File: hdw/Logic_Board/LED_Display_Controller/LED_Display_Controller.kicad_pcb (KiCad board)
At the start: 4 copper layers, 743 parts, among them J1101 USB_B_Mini, J1401 Encoder Ext, J1601 POS5P EXT, J1602 POS5P PGOOD, J1603 POS5P_THWN, J1604 POS5P_RUN, J201 +12V IN, J202 GND IN, J203 +12V IN AUX, J204 Master Power SW, J2901 STRING 1, J2902 STRING 2, J2903 STRING 3, J2904 STRING 4, J3001 USB UART, J3002 WIFI UART, J3003 FLASH SPI, J3004 Panel TP, J501 PICKIT3, J901 ESP8266 Socket, Q201 IPC100N04S51R7ATMA1, Q202 IPC100N04S51R7ATMA1, Q501 BSS214NW, Q901 BSS214NW, SW1401 Display Enable, SW1402 Brightness/Enable, SW501 MRST, U1001 ISO7321C, U1101 LT6700-1-S6, U1102 FT234XD, U1103 74LVC1G06, U1104 TPD3S014DBVR, U1201 74LVC1G06, U1202 74LVC1G06, U1203 74LVC1G06, U1204 74LVC1G06, U1205 74LVC1G06, U1206 74LVC1G06, U1207 74LVC1G06, U1301 74LVC1G06, U1302 74LVC1G06, U1303 74LVC1G06, U1304 74LVC1G06, U1401 MAX6816, U1402 74LVC2G14, U1403 74LVC1G79, U1601 LM1117-ADJ, U1602 NUP2202, U1603 74LVC1G17, U1604 74LVC1G17, U1605 74LVC1G17, U1606 NUP2202, U1701 CY7C1010DV33, U1801 SST25PF020B, U1901 SST25PF020B, U2001 SST25PF020B, U201 LTC4365DDB, U2101 SST25PF020B, U2201 SST25PF020B, U2301 SST25PF020B, U2401 SST25PF020B, U2501 SST25PF020B, U2601 74HCT541, U2602 74HCT541, U2701 74HCT541, U2702 74HCT541, U2801 74LVC1G32, U2802 74HCT541, U301 LTC3605A_UF, U401 LTC3624DD, U601 PIC32MZ2048EFH144_IPL

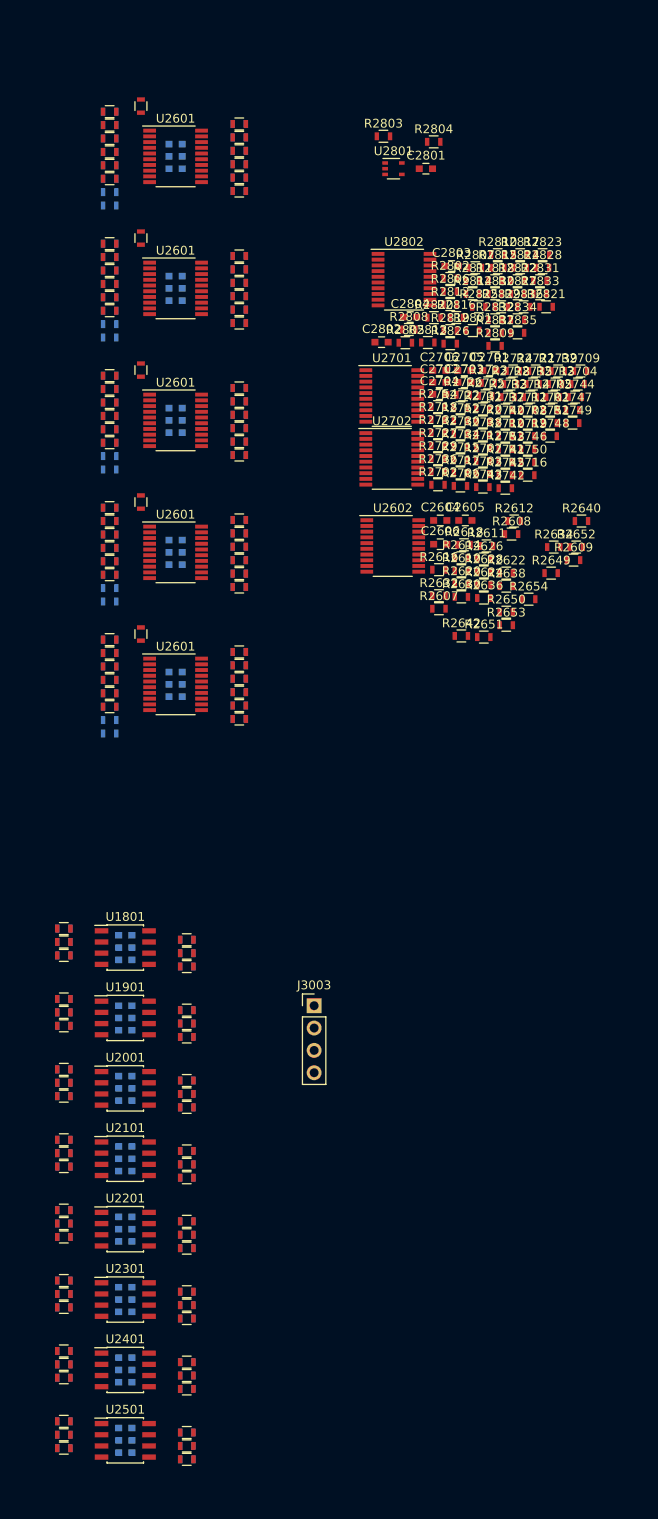
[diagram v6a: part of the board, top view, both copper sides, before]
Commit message: Fixed reference designators for level shifting/flash copies
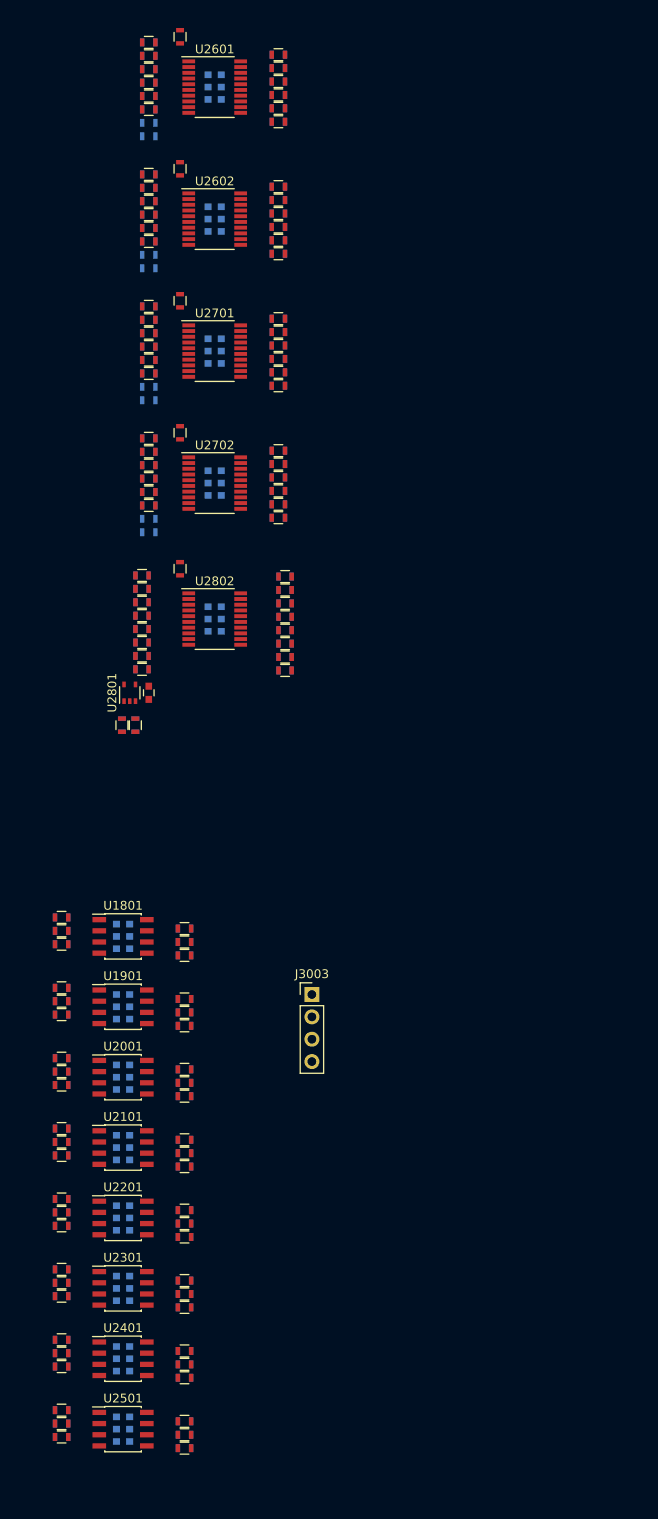
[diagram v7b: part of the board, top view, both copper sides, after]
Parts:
- removed the C2601 at (129.0, 96.7)
- removed the C2601 at (129.0, 81.7)
- removed the C2601 at (129.0, 66.7)
- removed the C2601 at (129.0, 51.7)
- removed the C2602 at (129.0, 98.1)
- removed the C2602 at (129.0, 83.1)
- removed the C2602 at (129.0, 68.1)
- removed the C2602 at (129.0, 53.1)
- removed the C2603 at (129.0, 99.5)
- removed the C2603 at (129.0, 84.5)
- removed the C2603 at (129.0, 69.5)
- removed the C2603 at (129.0, 54.5)
- removed the R2601 at (121.5, 93.0)
- removed the R2601 at (121.5, 78.0)
- removed the R2601 at (121.5, 63.0)
- removed the R2601 at (121.5, 48.0)
- removed the R2602 at (121.5, 94.5)
- removed the R2602 at (121.5, 79.5)
- removed the R2602 at (121.5, 64.5)
- removed the R2602 at (121.5, 49.5)
- removed the R2603 at (121.5, 96.1)
- removed the R2603 at (121.5, 81.1)
- removed the R2603 at (121.5, 66.1)
- removed the R2603 at (121.5, 51.1)
- removed the R2604 at (121.5, 97.6)
- removed the R2604 at (121.5, 82.6)
- removed the R2604 at (121.5, 67.6)
- removed the R2604 at (121.5, 52.6)
- removed the R2605 at (121.5, 99.1)
- removed the R2605 at (121.5, 84.1)
- removed the R2605 at (121.5, 69.1)
- removed the R2605 at (121.5, 54.1)
- removed the R2606 at (121.5, 100.6)
- removed the R2606 at (121.5, 85.6)
- removed the R2606 at (121.5, 70.6)
- removed the R2606 at (121.5, 55.6)
- removed the R2613 at (125.1, 92.4)
- removed the R2613 at (125.1, 77.4)
- removed the R2613 at (125.1, 62.4)
- removed the R2613 at (125.1, 47.4)
- removed the R2615 at (121.5, 93.0)
- removed the R2615 at (121.5, 78.0)
- removed the R2615 at (121.5, 63.0)
- removed the R2615 at (121.5, 48.0)
- removed the R2617 at (121.5, 94.5)
- removed the R2617 at (121.5, 79.5)
- removed the R2617 at (121.5, 64.5)
- removed the R2617 at (121.5, 49.5)
- removed the R2619 at (121.5, 96.1)
- removed the R2619 at (121.5, 81.1)
- removed the R2619 at (121.5, 66.1)
- removed the R2619 at (121.5, 51.1)
- removed the R2621 at (121.5, 97.6)
- removed the R2621 at (121.5, 82.6)
- removed the R2621 at (121.5, 67.6)
- removed the R2621 at (121.5, 52.6)
- removed the R2623 at (121.5, 99.1)
- removed the R2623 at (121.5, 84.1)
- removed the R2623 at (121.5, 69.1)
- removed the R2623 at (121.5, 54.1)
- removed the R2625 at (121.5, 100.6)
- removed the R2625 at (121.5, 85.6)
- removed the R2625 at (121.5, 70.6)
- removed the R2625 at (121.5, 55.6)
- removed the R2627 at (121.5, 102.2)
- removed the R2627 at (121.5, 87.2)
- removed the R2627 at (121.5, 72.2)
- removed the R2627 at (121.5, 57.2)
- removed the R2629 at (121.5, 103.7)
- removed the R2629 at (121.5, 88.7)
- removed the R2629 at (121.5, 73.7)
- removed the R2629 at (121.5, 58.7)
- removed the R2631 at (136.3, 102.0)
- removed the R2631 at (136.3, 87.0)
- removed the R2631 at (136.3, 72.0)
- removed the R2631 at (136.3, 57.0)
- removed the R2633 at (136.3, 100.5)
- removed the R2633 at (136.3, 85.5)
- removed the R2633 at (136.3, 70.5)
- removed the R2633 at (136.3, 55.5)
- removed the R2635 at (136.3, 99.0)
- removed the R2635 at (136.3, 84.0)
- removed the R2635 at (136.3, 69.0)
- removed the R2635 at (136.3, 54.0)
- removed the R2637 at (136.3, 97.5)
- removed the R2637 at (136.3, 82.5)
- removed the R2637 at (136.3, 67.5)
- removed the R2637 at (136.3, 52.5)
- removed the R2639 at (136.3, 95.9)
- removed the R2639 at (136.3, 80.9)
- removed the R2639 at (136.3, 65.9)
- removed the R2639 at (136.3, 50.9)
- removed the R2641 at (136.3, 94.4)
- removed the R2641 at (136.3, 79.4)
- removed the R2641 at (136.3, 64.4)
- removed the R2641 at (136.3, 49.4)
- removed the R2643 at (136.3, 94.4)
- removed the R2643 at (136.3, 79.4)
- removed the R2643 at (136.3, 64.4)
- removed the R2643 at (136.3, 49.4)
- removed the R2644 at (136.3, 95.9)
- removed the R2644 at (136.3, 80.9)
- removed the R2644 at (136.3, 65.9)
- removed the R2644 at (136.3, 50.9)
- removed the R2645 at (136.3, 97.5)
- removed the R2645 at (136.3, 82.5)
- removed the R2645 at (136.3, 67.5)
- removed the R2645 at (136.3, 52.5)
- removed the R2646 at (136.3, 99.0)
- removed the R2646 at (136.3, 84.0)
- removed the R2646 at (136.3, 69.0)
- removed the R2646 at (136.3, 54.0)
- removed the R2647 at (136.3, 100.5)
- removed the R2647 at (136.3, 85.5)
- removed the R2647 at (136.3, 70.5)
- removed the R2647 at (136.3, 55.5)
- removed the R2648 at (136.3, 102.0)
- removed the R2648 at (136.3, 87.0)
- removed the R2648 at (136.3, 72.0)
- removed the R2648 at (136.3, 57.0)
- removed the U2601 at (129.0, 98.1)
- removed the U2601 at (129.0, 83.1)
- removed the U2601 at (129.0, 68.1)
- removed the U2601 at (129.0, 53.1)
- C1901, C1902, C1903, C2001, C2002, C2003, C2101, C2102, C2103, C2201, C2202, C2203, C2301, C2302, C2303, C2401, C2402, C2403, C2501, C2502, C2503, R1906, R1907, R1908, R1909, R1910, R1911, R2006, R2007, R2008, R2009, R2010, R2011, R2106, R2107, R2108, R2109, R2110, R2111, R2206, R2207, R2208, R2209, R2210, R2211, R2306, R2307, R2308, R2309, R2310, R2311, R2406, R2407, R2408, R2409, R2410, R2411, R2506, R2507, R2508, R2509, R2510, R2511: moved to F.Cu
- C2604, C2605, C2606, C2802, C2803, C2804, R2616, R2618, R2620, R2622, R2624, R2626, R2628, R2630, R2632, R2634, R2636, R2638, R2640, R2642, R2803, R2804, R2814, R2815, R2816, R2817, R2818, R2819, R2820, R2821, R2822, R2823, R2824, R2825, R2826, R2827, R2828, R2829: moved to B.Cu
- moved R2804 74.5 mm to (124.5, 102.7), turned to 270 degrees
- moved R2803 73.2 mm to (122.9, 102.7), turned to 90 degrees
- moved C2801 67.4 mm to (126.0, 99.1), turned to 270 degrees
- moved U2801 66.7 mm to (123.8, 99.1), turned to 90 degrees
- moved R2609 63.2 mm to (126.0, 43.2)
- moved R2802 62.1 mm to (124.5, 102.7), turned to 90 degrees
- moved R2821 61.7 mm to (125.2, 96.4)
- moved R2801 60.0 mm to (122.9, 102.7), turned to 90 degrees
- moved R2810 59.8 mm to (125.2, 93.3)
- moved R2817 59.4 mm to (125.2, 90.3), turned to 180 degrees
- moved R2607 59.4 mm to (126.0, 40.1)
- moved R2622 57.5 mm to (126.0, 44.7), turned to 180 degrees
- moved R2608 57.0 mm to (126.0, 41.7)
- moved R2811 56.8 mm to (125.2, 94.9)
- moved R2818 56.4 mm to (125.2, 91.8), turned to 180 degrees
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
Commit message: Added board outline and placed mounting holes/IDC connectors
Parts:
- J2901, J2902, J2903, J2904: moved to B.Cu
- moved C1301 494.4 mm to (539.0, 162.9)
- moved C310 494.4 mm to (726.4, 250.7)
- moved C403 494.4 mm to (649.2, 236.1)
- moved C604 494.4 mm to (583.6, 77.1)
- moved C903 494.4 mm to (734.7, 210.4)
- moved D1303 494.4 mm to (563.1, 161.5)
- moved L401 494.4 mm to (653.8, 233.4)
- moved Q201 494.4 mm to (602.5, 239.3)
- moved Q901 494.4 mm to (729.5, 202.1)
- moved R1303 494.4 mm to (563.1, 159.9)
- moved R2613 494.4 mm to (623.6, 43.6)
- moved R2614 494.4 mm to (623.6, 58.6)
- moved R2713 494.4 mm to (623.6, 73.6)
- moved R2714 494.4 mm to (623.6, 88.6)
- moved R2813 494.4 mm to (623.6, 104.0)
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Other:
- board outline added: 400 x 100 mm
- board text added: "Cool stuff to add: USB COM port settings near connector Layer count Copper MU Logo Team member names Project name Manufacturer logos KiCAD logo LED labels Connector Labels Test point labels Input voltage polarity Output data signal labels Functional block labels? ESD warning Heat warning Black and white picture of group in silkscreen? Design rule / stackup notes"
- board text removed: "Cool stuff to add: USB COM port settings near connector Layer count Copper MU Logo Team member names Project name Manufacturer logos KiCAD logo LED labels Connector Labels Test point labels Input voltage polarity Output data signal labels Functional block labels? ESD warning Heat warning Black and white picture of group in silkscreen?"
- board text removed: "TO DO: Change Ref Des's"
